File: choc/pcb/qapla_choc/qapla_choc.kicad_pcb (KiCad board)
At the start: 2 copper layers, 154.4 x 126.1 mm, 72 parts

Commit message: Finalize choc case and pcb design
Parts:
- moved MH2 0.50 mm to (248.4, 84.7)
- moved D5 0.05 mm to (163.0, 85.0)
- moved D6 0.05 mm to (160.1, 51.2)
- moved D1 0.05 mm to (127.3, 102.8)
- moved D2 0.05 mm to (121.4, 69.3)
- moved D13 0.05 mm to (127.7, 105.1)
- moved D14 0.05 mm to (121.8, 71.6)
- moved D15 0.05 mm to (145.4, 102.0)
- moved D16 0.05 mm to (139.5, 68.5)
- moved D3 0.05 mm to (145.0, 99.6)
- moved D4 0.05 mm to (139.1, 66.2)
- moved D28 0.05 mm to (219.1, 115.8)
- moved D27 0.05 mm to (206.8, 113.0)
- moved D10 0.05 mm to (200.9, 50.0)
- moved D12 0.05 mm to (218.9, 52.5)
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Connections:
- _3 pad 3: GND -> P4

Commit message: Changing battery LED net
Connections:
- _3 pad 3: P4 -> P21
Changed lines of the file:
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@@
     (fp_line (start -1.5 -0.625) (end -1.5 0.625) (stroke (width 0.1) (type solid)) (layer "B.Fab"))
     (fp_line (start -1.5 0.625) (end -3.5 0.625) (stroke (width 0.1) (type solid)) (layer "B.Fab"))
-    (pad "3" thru_hole roundrect (at -3.5 0) (size 1.2 1.4) (drill 0.3) (layers "*.Cu" "*.Paste" "*.Mask") (roundrect_rratio 0.208333) (net 53 "P4"))
+    (pad "3" thru_hole roundrect (at -3.5 0) (size 1.2 1.4) (drill 0.3) (layers "*.Cu" "*.Paste" "*.Mask") (roundrect_rratio 0.208333) (net 48 "P21"))
     (pad "4" thru_hole roundrect (at -1.5 0) (size 1.2 1.4) (drill 0.3) (layers "*.Cu" "*.Paste" "*.Mask") (roundrect_rratio 0.208333) (net 88 "_3_1"))
   )

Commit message: MX Keyboard has a batleth
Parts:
- removed the _3 at (232.4, 76.8) (x2)
- added _3: , R_0805_2012Metric_Pad1.20x1.40mm_HandSolder, F.Cu at (232.4, 76.8)
- added _3: , D_0805_2012Metric_Pad1.15x1.40mm_HandSolder, F.Cu at (232.4, 76.8)
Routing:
- net (no net): track 337.7 -> 0.00 mm
- net GND: track 0.00 -> 96.6 mm, vias 0 -> 2
- net P1: track 0.00 -> 71.9 mm, vias 0 -> 1
- net P21: track 0.00 -> 45.5 mm
- net P2: track 0.00 -> 41.0 mm, vias 0 -> 1
- net VCC: track 0.00 -> 40.9 mm, vias 0 -> 1
- net P3: track 0.00 -> 32.8 mm, vias 0 -> 2
- net RST: track 0.00 -> 31.1 mm, vias 0 -> 1
- net RAW: track 0.00 -> 17.7 mm
- net BAT_P: track 0.00 -> 15.6 mm
- net P10: track 0.00 -> 9.84 mm
- net P20: track 0.00 -> 9.84 mm
- net P19: track 0.00 -> 9.84 mm
- net P18: track 0.00 -> 9.84 mm
- net P16: track 0.00 -> 9.84 mm
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
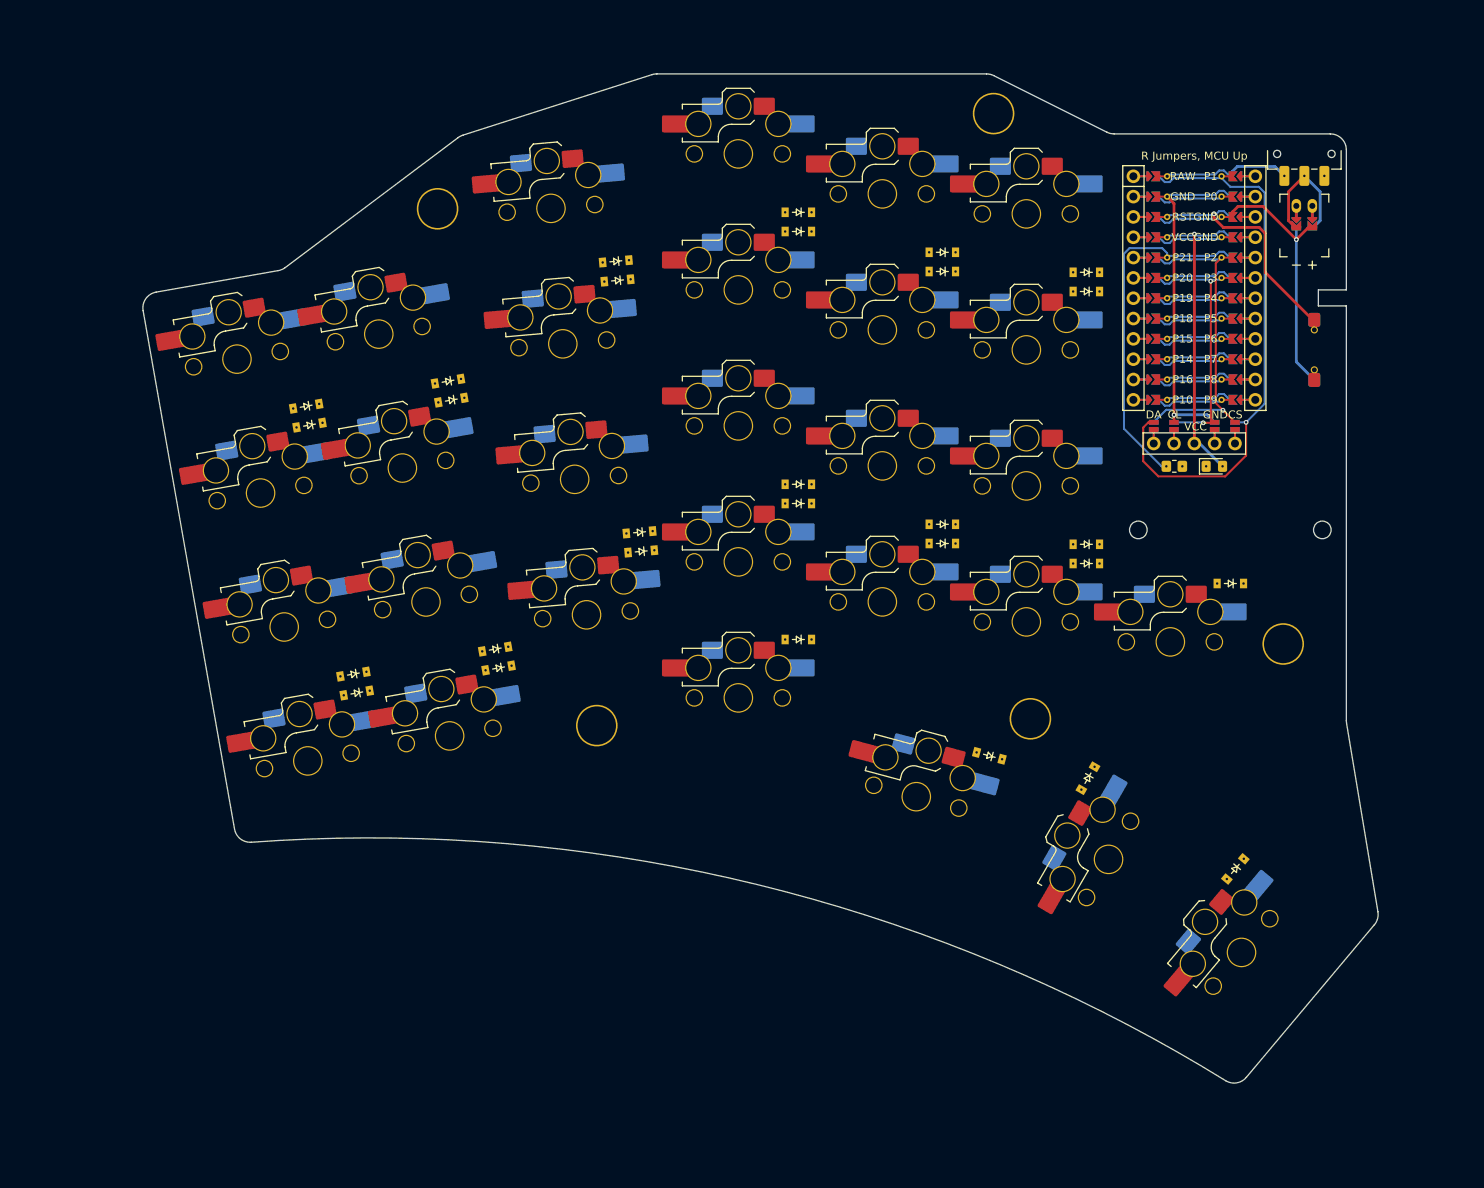
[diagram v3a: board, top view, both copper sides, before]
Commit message: Choc keyboard routing done
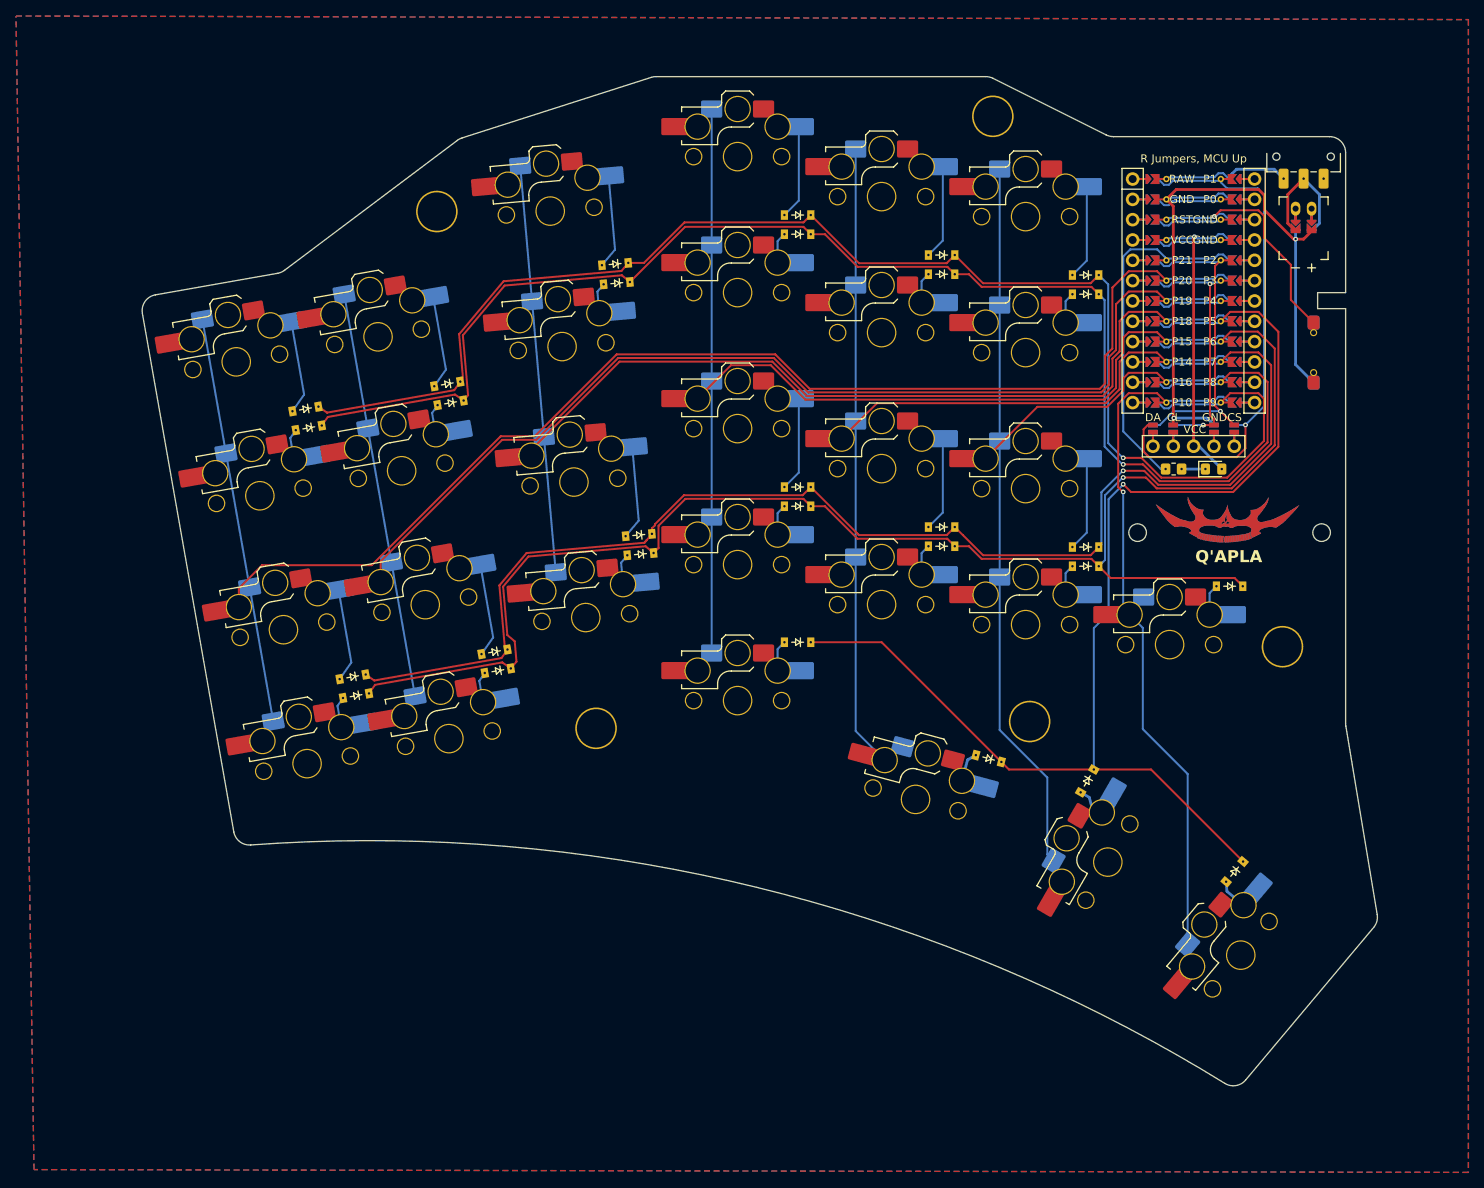
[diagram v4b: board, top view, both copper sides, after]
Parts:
- removed the _3 at (232.4, 76.8) (x2)
- added ?: , footprints:batleth, F.Cu at (236.6, 83.5)
- added _3: , D_0805_2012Metric_Pad1.15x1.40mm_HandSolder, F.Cu at (232.3, 77.1)
- added _3: , R_0805_2012Metric_Pad1.20x1.40mm_HandSolder, F.Cu at (232.3, 77.1)
- moved D10 0.35 mm to (200.8, 50.4)
- moved H1 0.35 mm to (137.7, 44.9)
- moved S1 0.35 mm to (121.5, 114.0)
- moved D29 0.35 mm to (237.4, 127.5)
- moved S5 0.35 mm to (139.2, 110.8)
- moved H5 0.35 mm to (243.4, 99.3)
- moved S9 0.35 mm to (156.3, 95.7)
- moved D1 0.35 mm to (127.2, 103.1)
- moved D25 0.35 mm to (218.8, 55.3)
- moved D23 0.35 mm to (200.8, 52.8)
- moved D13 0.35 mm to (127.6, 105.5)
- moved H2 0.35 mm to (157.6, 109.5)
- moved D20 0.35 mm to (182.8, 81.8)
- moved S22 0.35 mm to (211.3, 96.6)
- moved S7 0.35 mm to (133.3, 77.3)
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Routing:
- net P20: track 9.84 -> 206.1 mm
- net P6: track 9.83 -> 197.4 mm, vias 0 -> 1
- net P19: track 9.84 -> 185.0 mm
- net P8: track 9.83 -> 183.9 mm, vias 0 -> 1
- net P9: track 9.83 -> 181.6 mm, vias 0 -> 1
- net P7: track 9.83 -> 172.0 mm, vias 0 -> 1
- net P5: track 9.83 -> 157.6 mm, vias 0 -> 1
- net P18: track 9.84 -> 156.4 mm
- net P15: track 9.84 -> 147.1 mm
- net P14: track 9.84 -> 135.3 mm
- net P16: track 9.84 -> 127.5 mm
- net P10: track 9.84 -> 88.1 mm, vias 0 -> 1
- net pinky_num: track 0.00 -> 11.8 mm
- net inner_num: track 0.00 -> 11.8 mm
- net ring_num: track 0.00 -> 11.8 mm
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- added copper zone on B.Cu, net GND
- added copper zone on F.Cu, net GND
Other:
- board text added: "Q'APLA"
